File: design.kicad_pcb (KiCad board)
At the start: 2 copper layers, 54 x 71.1 mm, 55 parts, among them J2 Programming, J3 HRO_TYPE-C-31-M-12, SW1 SW_Push, SW2 EN, SW3 IO0, U1 TCK127BG, U2 AP3015, U3 ESP32-C3-WROOM-02-N4, U4 TTP223, U5 TTP223

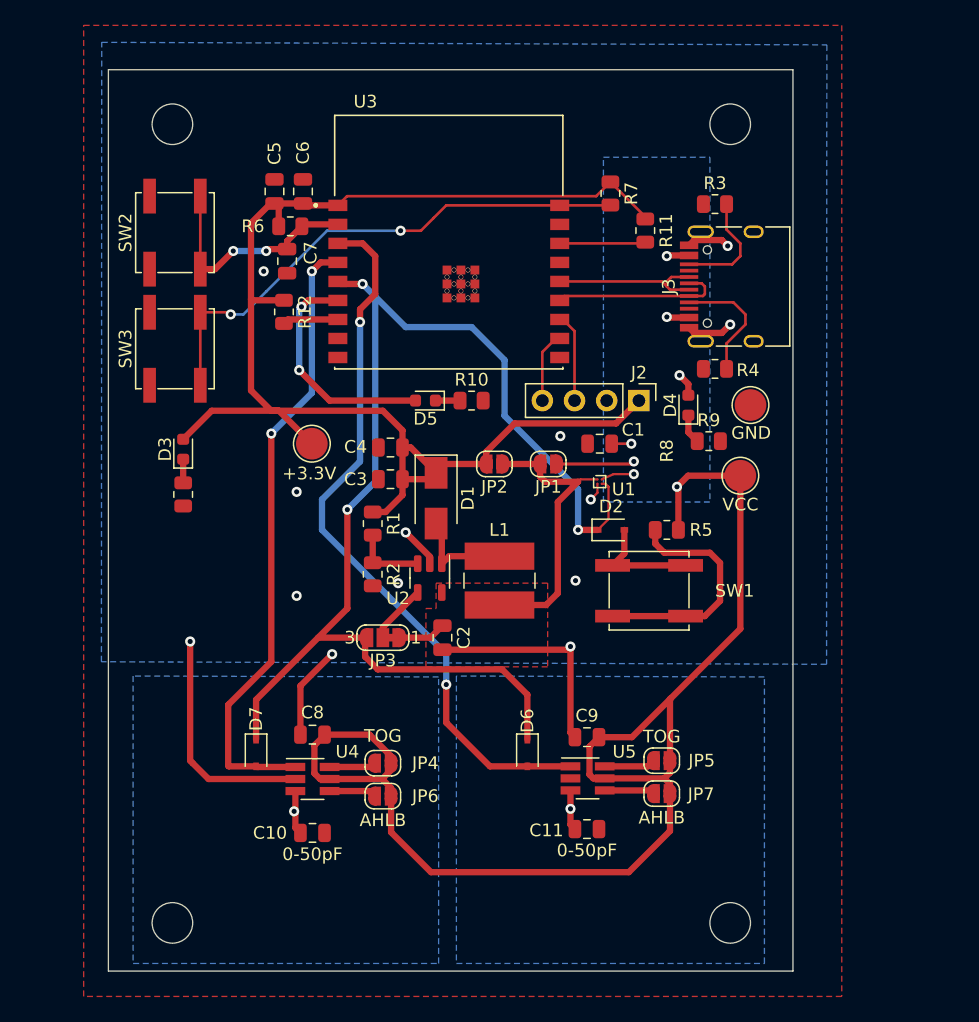
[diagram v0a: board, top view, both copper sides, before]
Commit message: cleaning up
silkscreen
info text
description
adding warning about unfinished input voltage rail
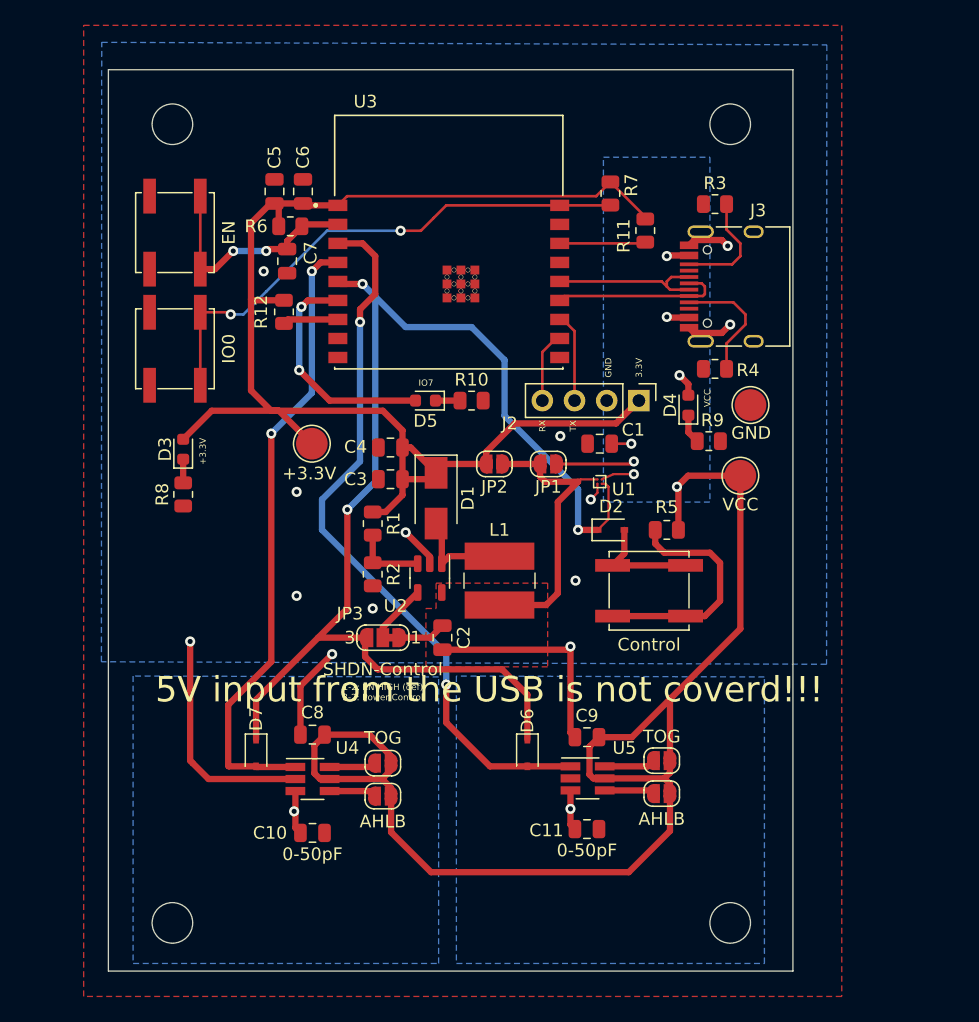
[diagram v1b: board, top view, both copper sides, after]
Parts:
- SW1: value SW_Push -> Control
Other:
- board text added: "+3.3V"
- board text added: "1-2: EN HIGH (def) 3-2: Power Control"
- board text added: "5V input from the USB is not coverd!!!"
- board text added: "GND 3.3V"
- board text added: "IO7"
- board text added: "RX TX"
- board text added: "TOG: LOW - Direct Mode HIGH - Toggle Mode AHLB: LOW - CMOS active high output HIGH - CMOS active low output"
- board text added: "VCC"

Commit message: Add USB to 3.3V and powerpath USB/Vbat
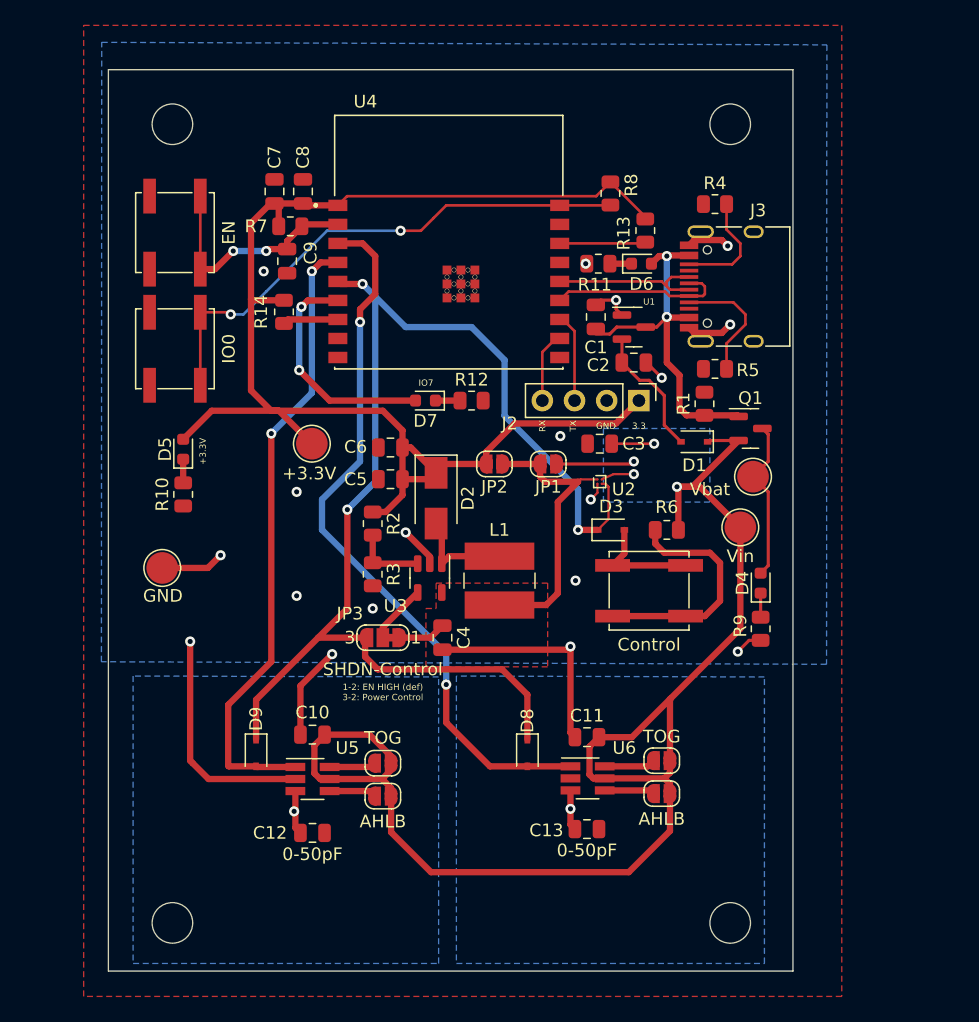
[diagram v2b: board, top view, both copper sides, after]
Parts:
- added C1: 1uF, Capacitor_SMD:C_0805_2012Metric, F.Cu at (152.6, 84.6)
- added C2: 1uF, Capacitor_SMD:C_0805_2012Metric, F.Cu at (155.6, 88.2)
- added D1: D_Small, Diode_SMD:D_SOD-323, F.Cu at (160.4, 94.5)
- added D4: LED, LED_SMD:LED_0603_1608Metric, F.Cu at (165.6, 105.6)
- added Q1: Q_PMOS_GSD, Package_TO_SOT_SMD:SOT-23, F.Cu at (164.8, 93.4)
- added R1: 100k, Resistor_SMD:R_0805_2012Metric, F.Cu at (161.2, 91.5)
- added R9: 330, Resistor_SMD:R_0805_2012Metric, F.Cu at (165.6, 109.2)
- added TP4: Vbat, TestPoint:TestPoint_Pad_D2.5mm, F.Cu at (165.0, 97.2)
- added U1: MCP1700-3302E_SOT23, Package_TO_SOT_SMD:SOT-23, F.Cu at (155.6, 85.4)
- TP2: value VCC -> Vin
- moved TP1 48.1 mm to (118.4, 104.4)
- moved R11 16.5 mm to (152.8, 80.4), turned to 180 degrees
- moved D6 11.8 mm to (156.2, 80.4), turned to 0 degrees
- moved TP2 4.08 mm to (164.0, 101.2)
- renumbered C8 to C10, C9 to C11, C10 to C12, C11 to C13, C1 to C3, C2 to C4, C3 to C5, C4 to C6, C5 to C7, C6 to C8, C7 to C9, D1 to D2, D2 to D3, D3 to D5, D4 to D6, D5 to D7, D6 to D8, D7 to D9, R8 to R10, R9 to R11, R10 to R12, R11 to R13, R12 to R14, R1 to R2, R2 to R3, R3 to R4, R4 to R5, R5 to R6, R6 to R7, R7 to R8, U1 to U2, U2 to U3, U3 to U4, U4 to U5, U5 to U6
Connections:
- C10 pad 1: Vbat -> Vin
- C11 pad 1: Vbat -> Vin
- C3 pad 1: Vbat -> Vin
- D6 pad 2: Vbat -> +5V
- J3 pad A4: Vbat -> +5V
- J3 pad A9: Vbat -> +5V
- J3 pad B4: Vbat -> +5V
- J3 pad B9: Vbat -> +5V
- JP1 pad 1: Vbat -> Vin
- JP4 pad 2: Vbat -> Vin
- JP5 pad 2: Vbat -> Vin
- JP6 pad 2: Vbat -> Vin
- JP7 pad 2: Vbat -> Vin
- R6 pad 1: Vbat -> Vin
- TP2 pad 1: Vbat -> Vin
- U2 pad A2: Vbat -> Vin
- U5 pad 5: Vbat -> Vin
- U6 pad 5: Vbat -> Vin
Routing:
- net Vin: track 0.00 -> 119.7 mm, vias 0 -> 4
- net Vbat: track 117.6 -> 12.8 mm, vias 7 -> 0
- net +5V: track 0.00 -> 28.5 mm, vias 0 -> 2
- net GND: track 55.0 -> 67.0 mm, vias 13 -> 18
- net Net-(C2-Pad1): track 0.00 -> 10.5 mm
- net Net-(D4-Pad1): track 0.00 -> 1.90 mm
- net Net-(D6-Pad1): track 2.34 -> 1.70 mm
- added copper zone on B.Cu, net Vin
- removed copper zone on B.Cu, net Vbat
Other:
- board text added: "3.3"
- board text added: "GND"
- board text removed: "5V input from the USB is not coverd!!!"
- board text removed: "GND 3.3V"
- board text removed: "VCC"

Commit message: checklist + final touchup SCH/PCB
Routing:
- net GND: track 67.0 -> 68.9 mm, vias 18 -> 20
- net IO2: track 6.79 -> 7.70 mm
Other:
- board text added: "5V"
- board text added: "D+"
- board text added: "D-"
- board text added: "EN"
- board text added: "IO0"
- board text added: "IO1"
- board text added: "IO10"
- board text added: "IO2"
- board text added: "IO4"
- board text added: "IO5"
- board text added: "IO6"
- board text added: "IO8"
- board text added: "IO9"
- board text added: "RX"
- board text added: "TX"
- board text added: "short for no Regulator"
- board text added: "short for no switch"

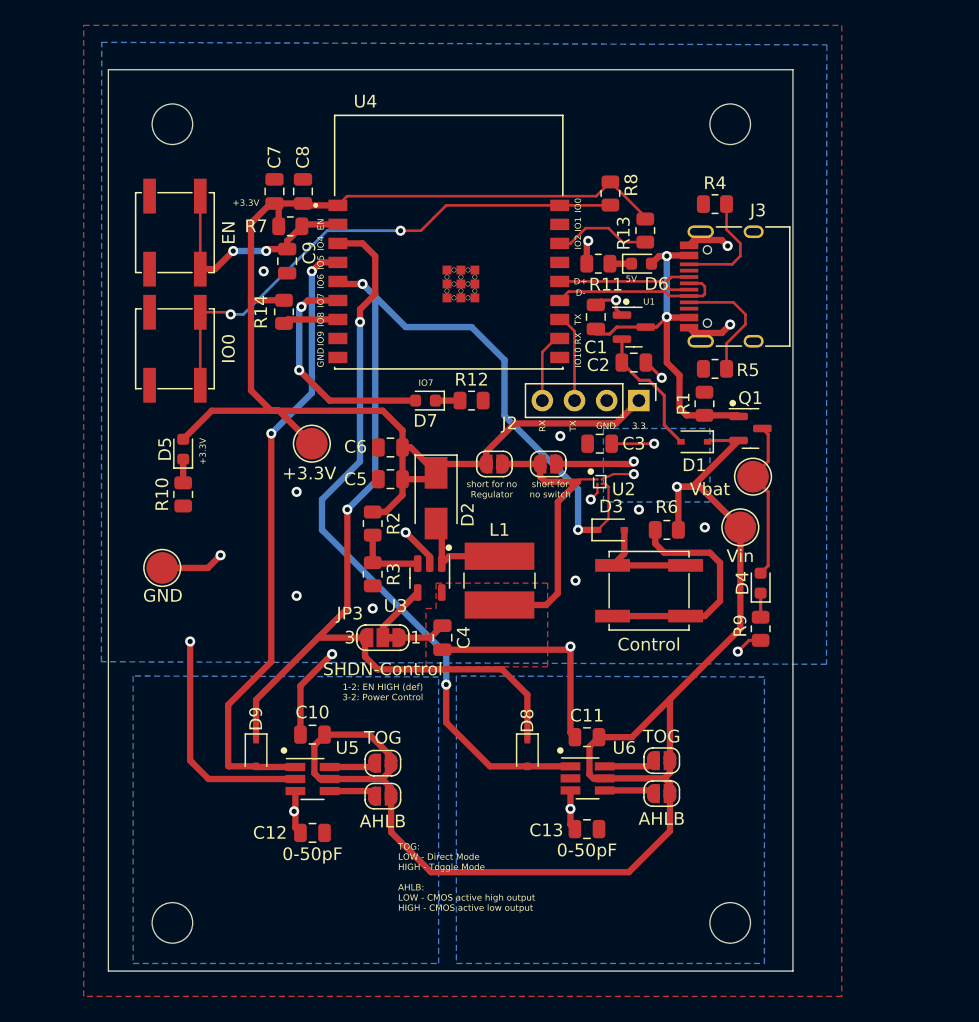
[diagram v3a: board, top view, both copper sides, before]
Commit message: rounded corners + mounting holes with copper
closes #7
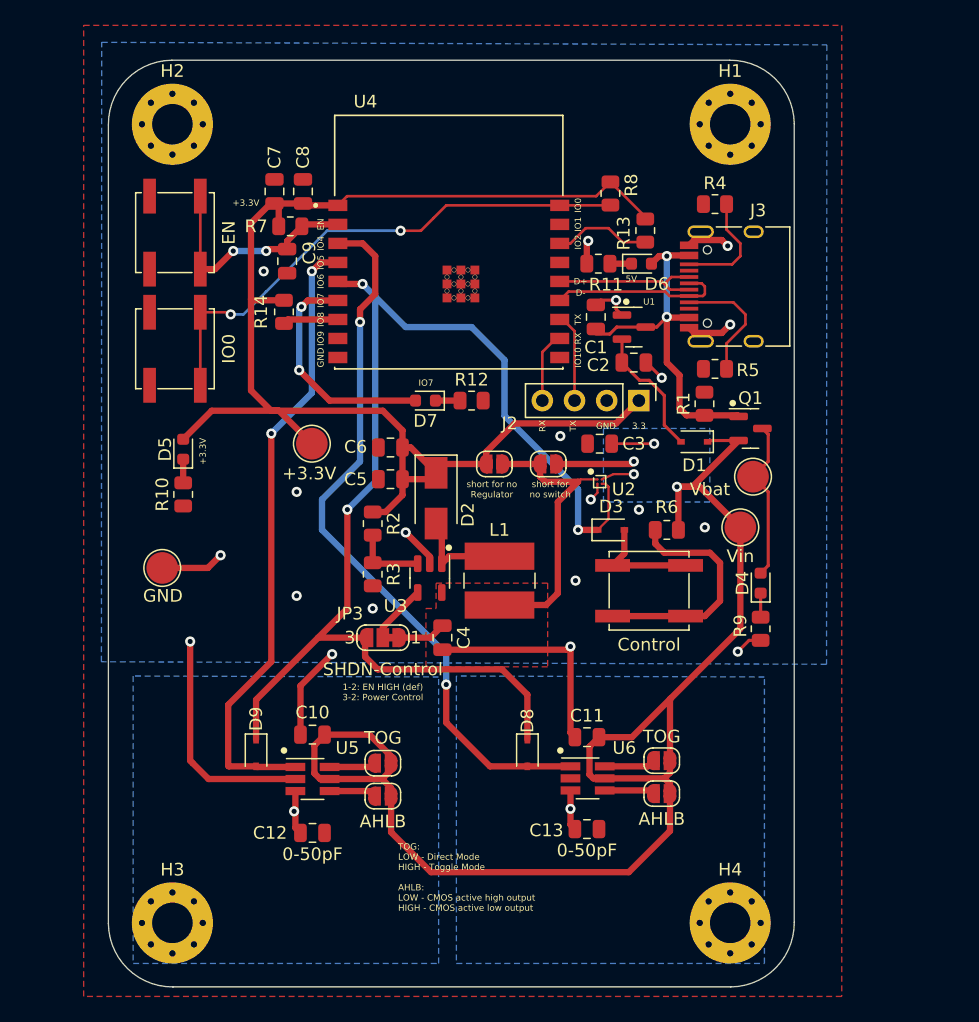
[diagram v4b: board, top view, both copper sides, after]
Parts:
- H1, H2, H3, H4: footprint MountingHole:MountingHole_3.2mm_M3 -> MountingHole:MountingHole_3.2mm_M3_Pad_Via
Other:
- board size 54 x 71.1 mm -> 54.1 x 73.1 mm

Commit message: move silksreen add clearance to m3 mounting pads
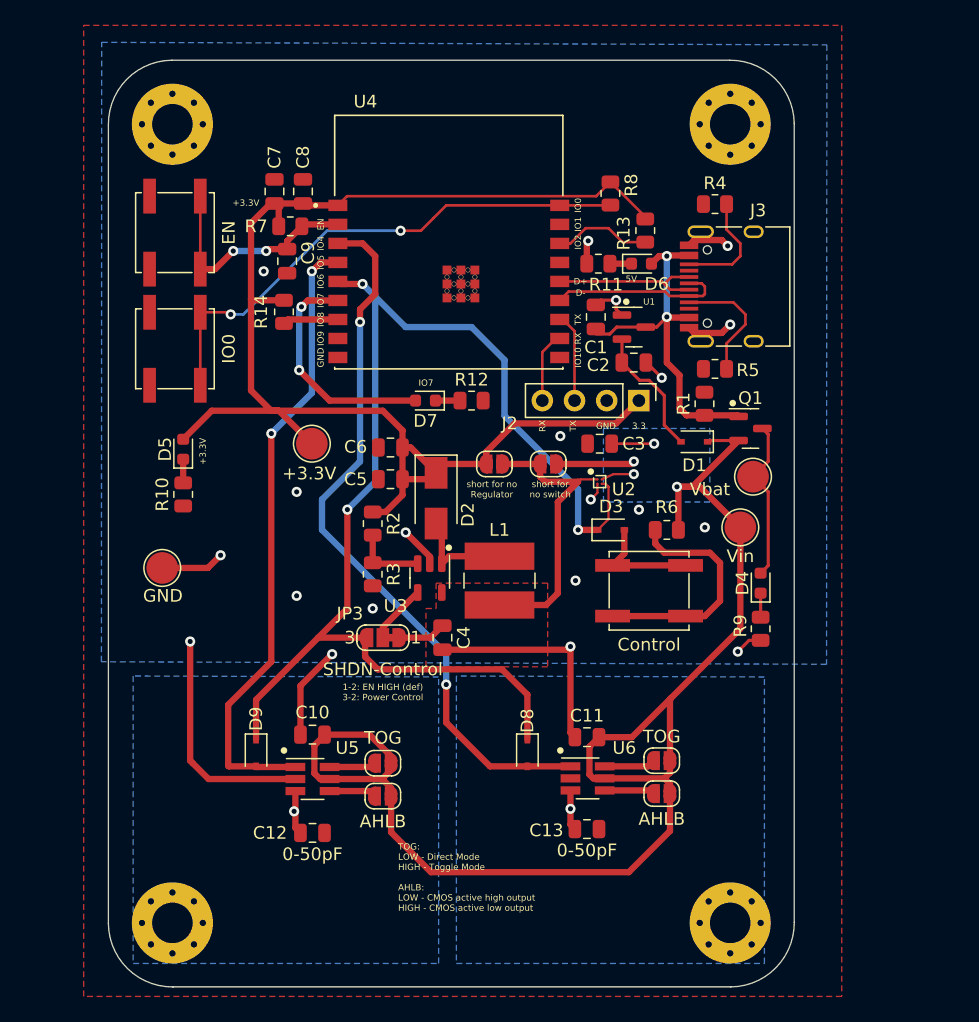
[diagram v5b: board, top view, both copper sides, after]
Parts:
- turned H3 to 90 degrees
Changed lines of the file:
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@@
     (property "Sheetname" "")
     (attr exclude_from_pos_files)
-    (fp_text reference "H2" (at 0 -4.2) (layer "F.SilkS")
+    (fp_text reference "H2" (at 0 -4.2) (layer "F.SilkS") hide
       (effects (font (size 1 1) (thickness 0.15)))
     )
@@
     (property "Sheetname" "")
     (attr exclude_from_pos_files)
-    (fp_text reference "H1" (at 0 -4.2) (layer "F.SilkS")
+    (fp_text reference "H1" (at 0 -4.2) (layer "F.SilkS") hide
       (effects (font (size 1 1) (thickness 0.15)))
     )
@@
   )
   (footprint "MountingHole:MountingHole_3.2mm_M3_Pad_Via" (layer "F.Cu")
-    (at 119.2 132.4)
+    (at 119.2 132.4 90)
     (descr "Mounting Hole 3.2mm, M3")
     (tags "mounting hole 3.2mm m3")
     (property "Sheetfile" "File: design.kicad_sch")
     (property "Sheetname" "")
+    (clearance 0.5)
     (attr exclude_from_pos_files)
-    (fp_text reference "H3" (at 0 -4.2) (layer "F.SilkS")
-      (effects (font (size 1 1) (thickness 0.15)))
-    )
-    (fp_text value "MountingHole" (at 0 4.2) (layer "F.Fab")
-      (effects (font (size 1 1) (thickness 0.15)))
-    )
-    (fp_text user "${REFERENCE}" (at 0 0) (layer "F.Fab")
+    (fp_text reference "H3" (at 0 -4.2 90) (layer "F.SilkS") hide
+      (effects (font (size 1 1) (thickness 0.15)))
+    )
+    (fp_text value "MountingHole" (at 0 4.2 90) (layer "F.Fab")
+      (effects (font (size 1 1) (thickness 0.15)))
+    )
+    (fp_text user "${REFERENCE}" (at 0 0 90) (layer "F.Fab")
       (effects (font (size 1 1) (thickness 0.15)))
     )
     (fp_circle (center 0 0) (end 3.2 0) (layer "Cmts.User") (width 0.15) (fill none))
     (fp_circle (center 0 0) (end 3.45 0) (layer "F.CrtYd") (width 0.05) (fill none))
-    (pad "1" thru_hole circle (at -2.4 0) (size 0.8 0.8) (drill 0.5) (layers *.Cu *.Mask))
-    (pad "1" thru_hole circle (at 0 0) (size 6.4 6.4) (drill 3.2) (layers *.Cu *.Mask))
-    (pad "1" thru_hole circle (at 0 -2.4) (size 0.8 0.8) (drill 0.5) (layers *.Cu *.Mask))
-    (pad "1" thru_hole circle (at -1.697056 1.697056) (size 0.8 0.8) (drill 0.5) (layers *.Cu *.Mask))
-    (pad "1" thru_hole circle (at 1.697056 -1.697056) (size 0.8 0.8) (drill 0.5) (layers *.Cu *.Mask))
-    (pad "1" thru_hole circle (at -1.697056 -1.697056) (size 0.8 0.8) (drill 0.5) (layers *.Cu *.Mask))
-    (pad "1" thru_hole circle (at 1.697056 1.697056) (size 0.8 0.8) (drill 0.5) (layers *.Cu *.Mask))
-    (pad "1" thru_hole circle (at 2.4 0) (size 0.8 0.8) (drill 0.5) (layers *.Cu *.Mask))
-    (pad "1" thru_hole circle (at 0 2.4) (size 0.8 0.8) (drill 0.5) (layers *.Cu *.Mask))
+    (pad "1" thru_hole circle (at -2.4 0 90) (size 0.8 0.8) (drill 0.5) (layers *.Cu *.Mask))
+    (pad "1" thru_hole circle (at 0 0 90) (size 6.4 6.4) (drill 3.2) (layers *.Cu *.Mask))
+    (pad "1" thru_hole circle (at 0 -2.4 90) (size 0.8 0.8) (drill 0.5) (layers *.Cu *.Mask))
+    (pad "1" thru_hole circle (at -1.697056 1.697056 90) (size 0.8 0.8) (drill 0.5) (layers *.Cu *.Mask))
+    (pad "1" thru_hole circle (at 1.697056 -1.697056 90) (size 0.8 0.8) (drill 0.5) (layers *.Cu *.Mask))
+    (pad "1" thru_hole circle (at -1.697056 -1.697056 90) (size 0.8 0.8) (drill 0.5) (layers *.Cu *.Mask))
+    (pad "1" thru_hole circle (at 1.697056 1.697056 90) (size 0.8 0.8) (drill 0.5) (layers *.Cu *.Mask))
+    (pad "1" thru_hole circle (at 2.4 0 90) (size 0.8 0.8) (drill 0.5) (layers *.Cu *.Mask))
+    (pad "1" thru_hole circle (at 0 2.4 90) (size 0.8 0.8) (drill 0.5) (layers *.Cu *.Mask))
   )
   (footprint "Resistor_SMD:R_0805_2012Metric" (layer "F.Cu")
@@
     (property "Sheetname" "")
     (attr exclude_from_pos_files)
-    (fp_text reference "H4" (at 0 -4.2) (layer "F.SilkS")
+    (fp_text reference "H4" (at 0 -4.2) (layer "F.SilkS") hide
       (effects (font (size 1 1) (thickness 0.15)))
     )
@@
     (property "Sheetname" "")
     (attr smd)
-    (fp_text reference "C9" (at -0.65 -1.75 90) (layer "F.SilkS")
-      (effects (font (size 1 1) (thickness 0.15)))
-    )
+    (fp_text reference "C9" (at -0.65 -1.65 90) (layer "F.SilkS")
+      (effects (font (size 1 1) (thickness 0.15)))
+    )
